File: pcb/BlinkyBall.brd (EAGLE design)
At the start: 18 x 18 mm, 18 parts, among them U1 Tiny85-20-SMT

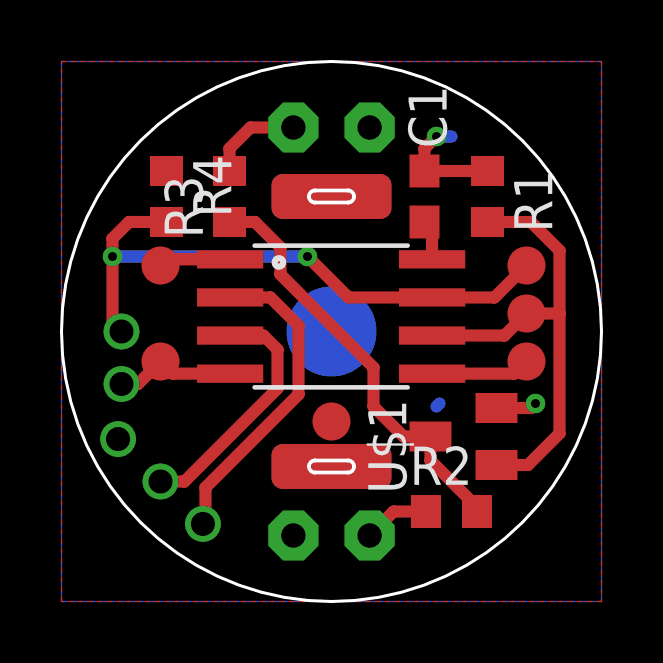
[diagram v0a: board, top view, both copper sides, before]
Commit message: RevC pcb design: rounded rect, switch IR pinout, space out test points
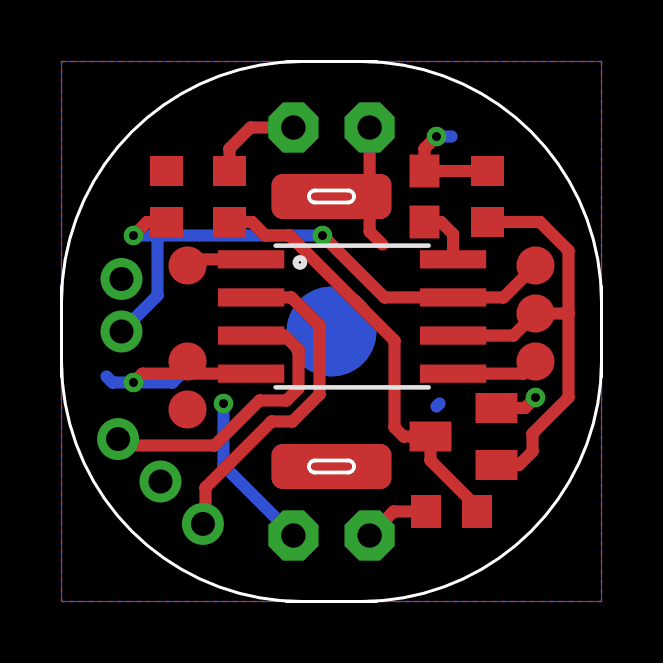
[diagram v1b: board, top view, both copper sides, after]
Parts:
- moved TP4 4.82 mm to (4.20, 6.40)
- moved TP5 0.90 mm to (4.20, 8.00)
- moved TP6 0.90 mm to (4.20, 11.2)
- moved U1 0.70 mm to (9.70, 9.50)
- moved TP1 0.30 mm to (15.8, 8.00)
- moved TP2 0.30 mm to (15.8, 9.60)
- moved TP3 0.30 mm to (15.8, 11.2)
- turned U$3 to 90 degrees
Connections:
- net GND: now also U$5.P$2; no longer U$5.P$3
- net IR_ENABLE: now also U$5.P$3; no longer U$5.P$2
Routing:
- net V_BATT: track 1.35 -> 12.8 mm, vias 0 -> 1
- net GND: track 9.52 -> 12.7 mm, vias 2 -> 3
- net IR_ENABLE: track 8.25 -> 9.96 mm
- net IR_SIGNAL: track 10.6 -> 11.3 mm
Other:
- outline, holes or cut-outs redrawn
- board text added: "RevC"
- board text removed: "RevB"

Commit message: More design tweaks
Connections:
- net GND: now also U$3.P$1; no longer U$3.P$2
- net WAKEUP: now also U$3.P$2; no longer U$3.P$1
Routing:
- net V_BATT: track 12.8 -> 9.42 mm, vias 1 -> 0
- net GND: track 12.7 -> 9.79 mm
- net WAKEUP: track 19.7 -> 18.4 mm, vias 2 -> 1
- net IR_ENABLE: track 9.96 -> 10.5 mm
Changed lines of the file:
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@@
 <setting verticaltext="up"/>
 </settings>
-<grid distance="0.5" unitdist="mm" unit="mm" style="lines" multiple="1" display="no" altdistance="0.1" altunitdist="mm" altunit="mm"/>
+<grid distance="0.5" unitdist="mm" unit="mm" style="lines" multiple="1" display="yes" altdistance="0.1" altunitdist="mm" altunit="mm"/>
 <layers>
 <layer number="1" name="Top" color="4" fill="1" visible="yes" active="yes"/>
@@
 <param name="mdSmdStop" value="0mil"/>
 <param name="msWidth" value="0.25mm"/>
-<param name="msDrill" value="0.3mm"/>
+<param name="msDrill" value="0.5mm"/>
 <param name="msMicroVia" value="13mil"/>
 <param name="msBlindViaRatio" value="0.5"/>
@@
 <param name="mlMinCreamFrame" value="0mil"/>
 <param name="mlMaxCreamFrame" value="0mil"/>
-<param name="mlViaStopLimit" value="0.35mm"/>
+<param name="mlViaStopLimit" value="0.55mm"/>
 <param name="srRoundness" value="0"/>
 <param name="srMinRoundness" value="0mil"/>
@@
 <contactref element="LED_TOP" pad="A"/>
 <contactref element="LED_BOT" pad="A"/>
-<via x="5.4" y="6.6" extent="1-16" drill="0.3"/>
-<wire x1="5.4" y1="6.6" x2="5.4" y2="4.53" width="0.4064" layer="16"/>
-<wire x1="5.4" y1="4.53" x2="7.73" y2="2.2" width="0.4064" layer="16"/>
 <wire x1="10.27" y1="15.8" x2="10.27" y2="13.77" width="0.4064" layer="1"/>
 <wire x1="10.27" y1="13.77" x2="10" y2="13.5" width="0.4064" layer="1"/>
@@
 <wire x1="10.27" y1="13.77" x2="10.27" y2="12.33" width="0.4064" layer="1"/>
 <wire x1="10.27" y1="12.33" x2="10.7" y2="11.9" width="0.4064" layer="1"/>
+<wire x1="9" y1="4.5" x2="9" y2="2.5" width="0.4064" layer="1"/>
 <wire x1="9" y1="13.5" x2="9" y2="13.5" width="0" layer="19" extent="1-16"/>
-<wire x1="5.4" y1="6.6" x2="10.7" y2="11.9" width="0" layer="19" extent="1-1"/>
+<wire x1="9" y1="4.5" x2="4.2" y2="6.4" width="0" layer="19" extent="1-16"/>
 <wire x1="9" y1="4.5" x2="9" y2="4.5" width="0" layer="19" extent="1-16"/>
 </signal>
@@
 <contactref element="U$1" pad="2"/>
 <contactref element="R1" pad="1"/>
-<wire x1="14.5" y1="6.45" x2="15.45" y2="6.45" width="0.4064" layer="1"/>
-<wire x1="15.45" y1="6.45" x2="15.8" y2="6.8" width="0.4064" layer="1"/>
-<via x="15.8" y="6.8" extent="1-16" drill="0.3"/>
+<wire x1="14.5" y1="6.45" x2="15.75" y2="6.45" width="0.4064" layer="1"/>
+<wire x1="15.75" y1="6.45" x2="15.9" y2="6.6" width="0.4064" layer="1"/>
+<via x="15.9" y="6.6" extent="1-16" drill="0.5"/>
 <wire x1="12.6" y1="6.6" x2="12.5" y2="6.5" width="0.4064" layer="16"/>
 <wire x1="14.2" y1="14.35" x2="12.1" y2="14.35" width="0.4064" layer="1"/>
-<wire x1="12.1" y1="14.35" x2="12.1" y2="15.1" width="0.4064" layer="1"/>
-<wire x1="12.1" y1="15.1" x2="12.5" y2="15.5" width="0.4064" layer="1"/>
-<via x="12.5" y="15.5" extent="1-16" drill="0.3"/>
-<wire x1="12.5" y1="15.5" x2="13" y2="15.5" width="0.4064" layer="16"/>
-<contactref element="U$3" pad="P$2"/>
-<via x="2.4" y="7.3" extent="1-16" drill="0.3"/>
-<wire x1="2.4" y1="7.3" x2="1.7" y2="7.3" width="0.4064" layer="16"/>
+<wire x1="12.1" y1="14.35" x2="12.1" y2="15.2" width="0.4064" layer="1"/>
+<wire x1="12.1" y1="15.2" x2="12.5" y2="15.6" width="0.4064" layer="1"/>
+<via x="12.5" y="15.6" extent="1-16" drill="0.5"/>
+<via x="4.1" y="9.4" extent="1-16" drill="0.5"/>
 <wire x1="1.7" y1="7.3" x2="1.5" y2="7.5" width="0.4064" layer="16"/>
-<wire x1="2.4" y1="7.3" x2="3.705" y2="7.3" width="0.4064" layer="16"/>
 <wire x1="3.705" y1="7.3" x2="4" y2="7.595" width="0.4064" layer="16"/>
 <wire x1="6.3218" y1="7.595" x2="4.2" y2="7.595" width="0.4064" layer="1"/>
-<wire x1="4.2" y1="7.595" x2="2.695" y2="7.595" width="0.4064" layer="1"/>
-<wire x1="2.695" y1="7.595" x2="2.4" y2="7.3" width="0.4064" layer="1"/>
 <wire x1="4.2" y1="8" x2="4.2" y2="7.595" width="0.4064" layer="1"/>
 <contactref element="U$5" pad="P$2"/>
+<contactref element="U$3" pad="P$1"/>
+<wire x1="4.1" y1="9.4" x2="4.1" y2="8.1" width="0.4064" layer="1"/>
+<wire x1="4.1" y1="8.1" x2="4.2" y2="8" width="0.4064" layer="1"/>
 </signal>
 <signal name="WAKEUP">
@@
 <contactref element="U1" pad="7"/>
 <contactref element="TP3" pad="P$1"/>
-<wire x1="13.0528" y1="10.135" x2="10.765" y2="10.135" width="0.4064" layer="1"/>
-<via x="8.7" y="12.2" extent="1-16" drill="0.3"/>
-<via x="2.4" y="12.2" extent="1-16" drill="0.3"/>
+<wire x1="13.0528" y1="10.135" x2="10.965" y2="10.135" width="0.4064" layer="1"/>
+<via x="9.1" y="12" extent="1-16" drill="0.5"/>
 <wire x1="13.0528" y1="10.135" x2="14.735" y2="10.135" width="0.4064" layer="1"/>
 <wire x1="14.735" y1="10.135" x2="15.8" y2="11.2" width="0.4064" layer="1"/>
-<contactref element="U$3" pad="P$1"/>
-<wire x1="10.765" y1="10.135" x2="8.7" y2="12.2" width="0.4064" layer="1"/>
+<wire x1="10.965" y1="10.135" x2="9.1" y2="12" width="0.4064" layer="1"/>
 <wire x1="3.5" y1="12.65" x2="2.85" y2="12.65" width="0.4064" layer="1"/>
-<wire x1="2.85" y1="12.65" x2="2.4" y2="12.2" width="0.4064" layer="1"/>
-<wire x1="2" y1="9" x2="3.2" y2="10.2" width="0.4064" layer="16"/>
-<wire x1="3.2" y1="10.2" x2="3.2" y2="12.2" width="0.4064" layer="16"/>
-<wire x1="2.4" y1="12.2" x2="3.2" y2="12.2" width="0.4064" layer="16"/>
-<wire x1="8.7" y1="12.2" x2="3.2" y2="12.2" width="0.4064" layer="16"/>
+<wire x1="2.85" y1="12.65" x2="2" y2="11.8" width="0.4064" layer="1"/>
+<contactref element="U$3" pad="P$2"/>
+<wire x1="2" y1="11.8" x2="2" y2="10.75" width="0.4064" layer="1"/>
+<wire x1="9.1" y1="12" x2="3.25" y2="12" width="0.4064" layer="16"/>
+<wire x1="3.25" y1="12" x2="2" y2="10.75" width="0.4064" layer="16"/>
 </signal>
 <signal name="LED_TOP">
@@
 <wire x1="15.95" y1="12.65" x2="16.9" y2="11.7" width="0.4064" layer="1"/>
 <wire x1="16.9" y1="11.7" x2="16.9" y2="9.6" width="0.4064" layer="1"/>
-<wire x1="16.9" y1="9.6" x2="16.9" y2="6.8" width="0.4064" layer="1"/>
-<wire x1="16.9" y1="6.8" x2="15.7" y2="5.6" width="0.4064" layer="1"/>
+<wire x1="16.9" y1="9.6" x2="16.9" y2="6.2" width="0.4064" layer="1"/>
+<wire x1="16.9" y1="6.2" x2="15.25" y2="4.55" width="0.4064" layer="1"/>
 <wire x1="14.5" y1="4.55" x2="15.25" y2="4.55" width="0.4064" layer="1"/>
-<wire x1="15.25" y1="4.55" x2="15.7" y2="5" width="0.4064" layer="1"/>
-<wire x1="15.7" y1="5" x2="15.7" y2="5.6" width="0.4064" layer="1"/>
 </signal>
 <signal name="YYYYY">
@@
 <wire x1="7.9" y1="8.4" x2="7.9" y2="7.1" width="0.4064" layer="1"/>
 <contactref element="U$5" pad="P$3"/>
-<wire x1="1.8857875" y1="5.4142125" x2="2.1" y2="5.2" width="0.4064" layer="1"/>
+<wire x1="1.50395" y1="5.79605" x2="2.1" y2="5.2" width="0.4064" layer="1"/>
 <wire x1="2.1" y1="5.2" x2="5.1" y2="5.2" width="0.4064" layer="1"/>
 <wire x1="7.9" y1="7.1" x2="7.5" y2="6.7" width="0.4064" layer="1"/>
@@
 <wire x1="7.665" y1="10.135" x2="8.6" y2="9.2" width="0.4064" layer="1"/>
 <contactref element="U$5" pad="P$1"/>
-<wire x1="4.8" y1="3.8" x2="4.8" y2="2.67156875" width="0.4064" layer="1"/>
-<wire x1="4.8" y1="2.67156875" x2="4.714215625" y2="2.585784375" width="0.4064" layer="1"/>
-<wire x1="4.8" y1="3.8" x2="7" y2="6" width="0.4064" layer="1"/>
+<wire x1="5.1" y1="4.1" x2="5.1" y2="2.3" width="0.4064" layer="1"/>
+<wire x1="5.1" y1="4.1" x2="7" y2="6" width="0.4064" layer="1"/>
 <wire x1="7" y1="6" x2="7.7" y2="6" width="0.4064" layer="1"/>
 <wire x1="7.7" y1="6" x2="8.6" y2="6.9" width="0.4064" layer="1"/>
 <wire x1="8.6" y1="6.9" x2="8.6" y2="9.2" width="0.4064" layer="1"/>
+<wire x1="5.1" y1="2.3" x2="5.096053125" y2="2.296053125" width="0.4064" layer="1"/>
+<wire x1="5.096053125" y1="2.296053125" x2="5.096053125" y2="2.203946875" width="0.4064" layer="1"/>
 </signal>
 <signal name="RESET">
